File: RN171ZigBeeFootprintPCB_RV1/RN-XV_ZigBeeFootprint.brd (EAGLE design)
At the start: 39.1 x 46.7 mm, 5 parts

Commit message: Connecting GND to the circuit
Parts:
- removed U$2: (no value), eka_logo:EKA_LOGO
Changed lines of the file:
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@@
 <?xml version="1.0" encoding="utf-8"?>
 <!DOCTYPE eagle SYSTEM "eagle.dtd">
-<eagle version="6.6.0">
+<eagle version="6.1">
 <drawing>
 <settings>
@@
 </class>
 </classes>
-<designrules name="default">
+<designrules>
 <description language="de">&lt;b&gt;EAGLE Design Rules&lt;/b&gt;
 &lt;p&gt;
@@
 <element name="J2" library="con-amp" package="10X08MTA" value="" x="29.21" y="35.8775" rot="R90"/>
 <element name="J3" library="con-amp" package="10X08MTA" value="" x="-2.7559" y="30.4546" rot="R90"/>
-<element name="U$2" library="eka_logo" package="EKA_LOGO" value="" x="6.6675" y="2.54"/>
 </elements>
 <signals>

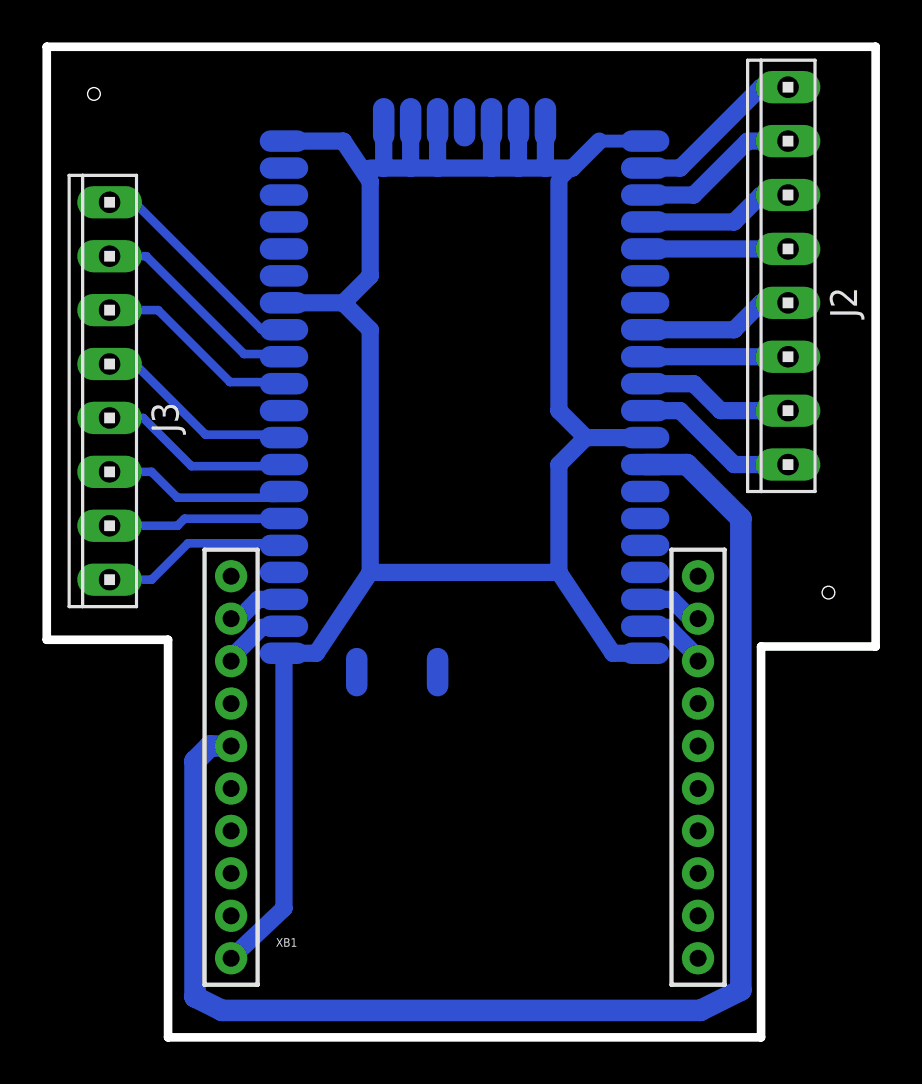
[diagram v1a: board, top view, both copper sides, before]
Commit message: Connecting RN171's 34 pin to VCC
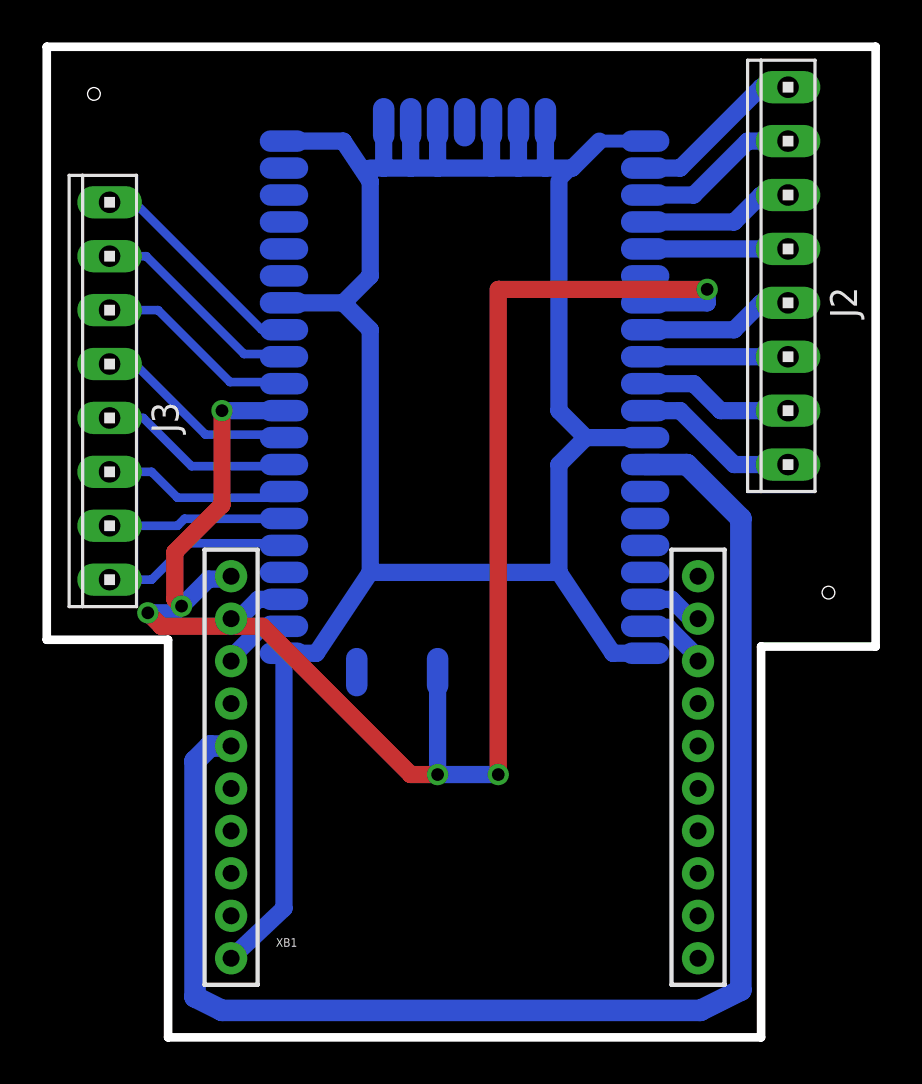
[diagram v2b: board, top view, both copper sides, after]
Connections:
- removed net VCC: XB1.1
- net VDD_3.3V: now also J1.34, J1.49, XB1.1
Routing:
- net VDD_3.3V: track 0.00 -> 78.6 mm, vias 0 -> 6
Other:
- board text added: "REV 1.0"
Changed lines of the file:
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@@
 <?xml version="1.0" encoding="utf-8"?>
 <!DOCTYPE eagle SYSTEM "eagle.dtd">
-<eagle version="6.1">
+<eagle version="6.6.0">
 <drawing>
 <settings>
@@
 <hole x="-3.4925" y="44.45" drill="0.6"/>
 <hole x="31.115" y="20.955" drill="0.6"/>
+<text x="9.525" y="3.175" size="1.778" layer="48">REV 1.0</text>
 </plain>
 <attributes>
@@
 </class>
 </classes>
-<designrules>
+<designrules name="default">
 <description language="de">&lt;b&gt;EAGLE Design Rules&lt;/b&gt;
 &lt;p&gt;
@@
 <wire x1="2.97" y1="17.8798" x2="2.97" y2="17.7272" width="0.8128" layer="16"/>
 </signal>
-<signal name="VCC">
-<contactref element="XB1" pad="1"/>
-</signal>
 <signal name="VDD_3.3V">
 <contactref element="J1" pad="10"/>
+<contactref element="J1" pad="49"/>
+<contactref element="XB1" pad="1"/>
+<wire x1="5.461" y1="29.5275" x2="2.54" y2="29.5275" width="0.8128" layer="16"/>
+<via x="2.54" y="29.5275" extent="1-16" drill="0.6" shape="square"/>
+<wire x1="2.54" y1="29.5275" x2="2.54" y2="25.0825" width="0.8128" layer="1"/>
+<wire x1="2.54" y1="25.0825" x2="0.3175" y2="22.86" width="0.8128" layer="1"/>
+<wire x1="0.3175" y1="22.86" x2="0.3175" y2="20.6375" width="0.8128" layer="1"/>
+<wire x1="0.3175" y1="20.6375" x2="0.635" y2="20.32" width="0.8128" layer="1"/>
+<via x="0.635" y="20.32" extent="1-16" drill="0.6" shape="square"/>
+<wire x1="0.635" y1="20.32" x2="1.905" y2="21.59" width="0.8128" layer="16"/>
+<wire x1="1.905" y1="21.59" x2="2.8328" y2="21.59" width="0.8128" layer="16"/>
+<wire x1="2.8328" y1="21.59" x2="2.97" y2="21.7272" width="0.8128" layer="16"/>
+<wire x1="12.7" y1="17.2085" x2="12.7" y2="12.3825" width="0.8128" layer="16"/>
+<via x="12.7" y="12.3825" extent="1-16" drill="0.6" shape="square"/>
+<wire x1="12.7" y1="12.3825" x2="11.43" y2="12.3825" width="0.8128" layer="1"/>
+<wire x1="11.43" y1="12.3825" x2="4.445" y2="19.3675" width="0.8128" layer="1"/>
+<wire x1="4.445" y1="19.3675" x2="-0.3175" y2="19.3675" width="0.8128" layer="1"/>
+<wire x1="-0.3175" y1="19.3675" x2="-0.9525" y2="20.0025" width="0.8128" layer="1"/>
+<via x="-0.9525" y="20.0025" extent="1-16" drill="0.6" shape="square"/>
+<wire x1="-0.9525" y1="20.0025" x2="0.3175" y2="20.0025" width="0.8128" layer="16"/>
+<wire x1="0.3175" y1="20.0025" x2="0.635" y2="20.32" width="0.8128" layer="16"/>
+<contactref element="J1" pad="34"/>
+<wire x1="22.479" y1="34.6075" x2="25.4" y2="34.6075" width="0.8128" layer="16"/>
+<wire x1="25.4" y1="34.6075" x2="25.4" y2="35.2425" width="0.8128" layer="16"/>
+<via x="25.4" y="35.2425" extent="1-16" drill="0.6" shape="square"/>
+<wire x1="25.4" y1="35.2425" x2="15.5575" y2="35.2425" width="0.8128" layer="1"/>
+<wire x1="15.5575" y1="35.2425" x2="15.5575" y2="12.3825" width="0.8128" layer="1"/>
+<via x="15.5575" y="12.3825" extent="1-16" drill="0.6" shape="square"/>
+<wire x1="15.5575" y1="12.3825" x2="12.7" y2="12.3825" width="0.8128" layer="16"/>
 </signal>
 <signal name="N$1">
